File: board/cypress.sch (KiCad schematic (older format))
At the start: 50 parts, among them J1 USB_MICRO_B, U1 CY7C68013A, U2 M25P16, X1 CRYSTAL

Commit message: Issue #1022 - Power supply & pic& SCHEMATIC SECTION.
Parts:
- added R308, R310, R311, R312: 100R, ~, symbol R
- added R309, R313: 330R, ~, symbol R
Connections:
- net at U1.45 (PD0/FD8): now also R308.1
- net at U1.46 (PD1/FD9): now also R309.1
- net at U1.47 (PD2/FD10): now also R310.1
- net at U1.48 (PD3/FD11): now also R311.1
- net at U1.49 (PD4/FD12): now also R312.1
- net RESET: now reaches U1.51 (PD6/FD14)
- net at U1.52 (PD7/FD15): now also R313.1
- new net DONE: R313.2
- new net PROG_B: R309.2
- new net TCK: R312.2
- new net TDO-USB/TDI-FPGA: R310.2
- new net TDO_FPGA/TDO-JTAG: R308.2
- new net TMS: R311.2
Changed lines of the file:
@@
 Sheet 2 8
 Title ""
-Date "14 mar 2014"
+Date "18 mar 2014"
 Rev ""
 Comp ""
@@
 Connection ~ 4600 6900
 NoConn ~ 2050 1650
+$Comp
+L R R308
+U 1 1 5329563E
+P 6100 3450
+F 0 "R308" V 6150 3650 40  0000 C CNN
+F 1 "100R" V 6107 3451 40  0000 C CNN
+F 2 "~" V 6030 3450 30  0000 C CNN
+F 3 "~" H 6100 3450 30  0000 C CNN
+	1    6100 3450
+	0    -1   -1   0
+$EndComp
+Wire Wire Line
+	5600 3450 5850 3450
+Wire Wire Line
+	5600 3650 5850 3650
+$Comp
+L R R310
+U 1 1 53295873
+P 6100 3650
+F 0 "R310" V 6150 3850 40  0000 C CNN
+F 1 "100R" V 6107 3651 40  0000 C CNN
+F 2 "~" V 6030 3650 30  0000 C CNN
+F 3 "~" H 6100 3650 30  0000 C CNN
+	1    6100 3650
+	0    -1   -1   0
+$EndComp
+$Comp
+L R R311
+U 1 1 53295931
+P 6100 3750
+F 0 "R311" V 6150 3950 40  0000 C CNN
+F 1 "100R" V 6107 3751 40  0000 C CNN
+F 2 "~" V 6030 3750 30  0000 C CNN
+F 3 "~" H 6100 3750 30  0000 C CNN
+	1    6100 3750
+	0    -1   -1   0
+$EndComp
+$Comp
+L R R312
+U 1 1 53295964
+P 6100 3850
+F 0 "R312" V 6150 4050 40  0000 C CNN
+F 1 "100R" V 6107 3851 40  0000 C CNN
+F 2 "~" V 6030 3850 30  0000 C CNN
+F 3 "~" H 6100 3850 30  0000 C CNN
+	1    6100 3850
+	0    -1   -1   0
+$EndComp
+Wire Wire Line
+	5600 3750 5850 3750
+Wire Wire Line
+	5600 3850 5850 3850
+Text HLabel 6350 3450 2    39   BiDi ~ 0
+TDO_FPGA/TDO-JTAG
+Text HLabel 6350 3650 2    39   BiDi ~ 0
+TDO-USB/TDI-FPGA
+Text HLabel 6350 3750 2    39   Input ~ 0
+TMS
+Text HLabel 6350 3850 2    39   Input ~ 0
+TCK
+$Comp
+L R R309
+U 1 1 5329986E
+P 6100 3550
+F 0 "R309" V 6150 3750 40  0000 C CNN
+F 1 "330R" V 6107 3551 40  0000 C CNN
+F 2 "~" V 6030 3550 30  0000 C CNN
+F 3 "~" H 6100 3550 30  0000 C CNN
+	1    6100 3550
+	0    -1   -1   0
+$EndComp
+Wire Wire Line
+	5600 3550 5850 3550
+Text HLabel 6350 3550 2    39   Input ~ 0
+PROG_B
+$Comp
+L R R313
+U 1 1 5329AA07
+P 6100 4150
+F 0 "R313" V 6150 4350 40  0000 C CNN
+F 1 "330R" V 6107 4151 40  0000 C CNN
+F 2 "~" V 6030 4150 30  0000 C CNN
+F 3 "~" H 6100 4150 30  0000 C CNN
+	1    6100 4150
+	0    -1   -1   0
+$EndComp
+Wire Wire Line
+	5600 4150 5850 4150
+Text HLabel 6350 4150 2    39   Input ~ 0
+DONE
+Wire Wire Line
+	5600 4050 5900 4050
+Text HLabel 5900 4050 2    39   Input ~ 0
+RESET
 $EndSCHEMATC

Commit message: Issue #1022 - Cypress
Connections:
- no-connect marks 4 -> 5
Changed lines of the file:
@@
 Text HLabel 5900 4050 2    39   Input ~ 0
 RESET
+NoConn ~ 5600 3950
 $EndSCHEMATC

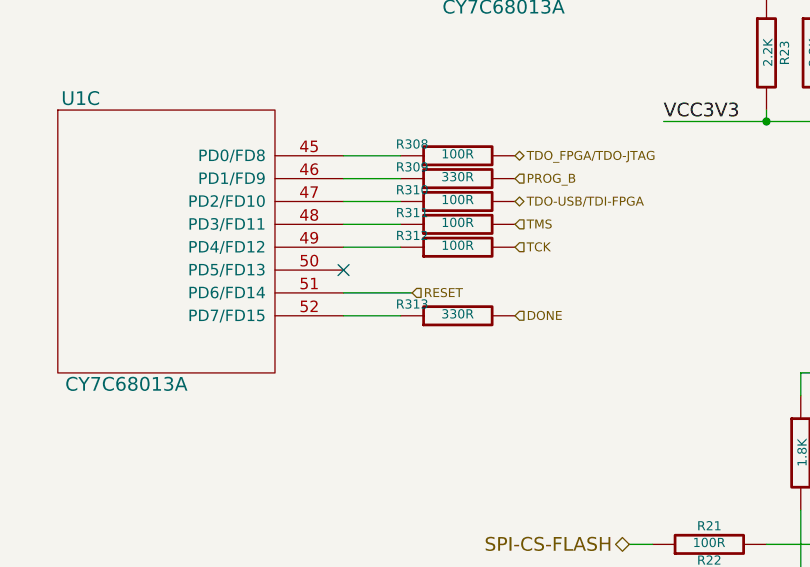
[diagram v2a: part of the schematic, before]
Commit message: Issue #1022 - Reset signals
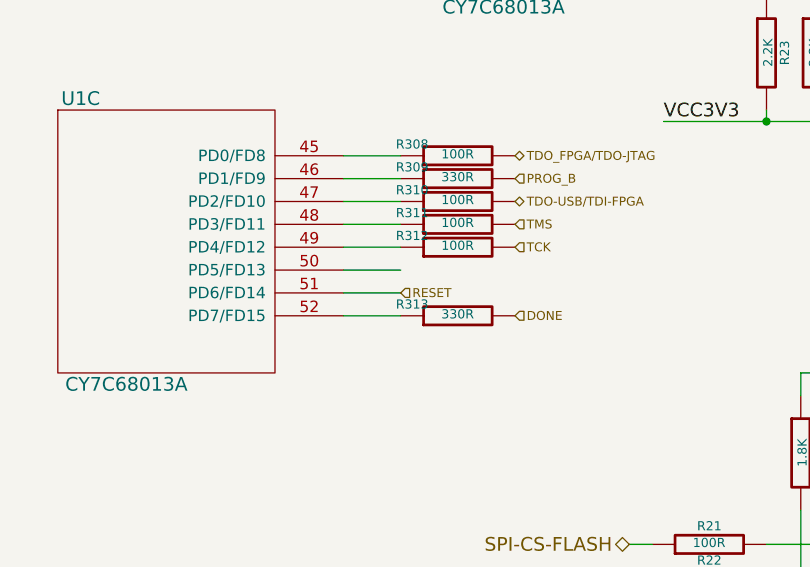
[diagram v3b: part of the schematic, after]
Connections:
- no-connect marks 5 -> 4
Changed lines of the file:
@@
 Sheet 2 8
 Title ""
-Date "18 mar 2014"
+Date "25 mar 2014"
 Rev ""
 Comp ""
@@
 Text HLabel 6350 4150 2    39   Input ~ 0
 DONE
-Wire Wire Line
-	5600 4050 5900 4050
-Text HLabel 5900 4050 2    39   Input ~ 0
+Text HLabel 5850 4050 2    39   Input ~ 0
 RESET
-NoConn ~ 5600 3950
+Wire Wire Line
+	5600 3950 5850 3950
+Wire Wire Line
+	5600 4050 5850 4050
 $EndSCHEMATC

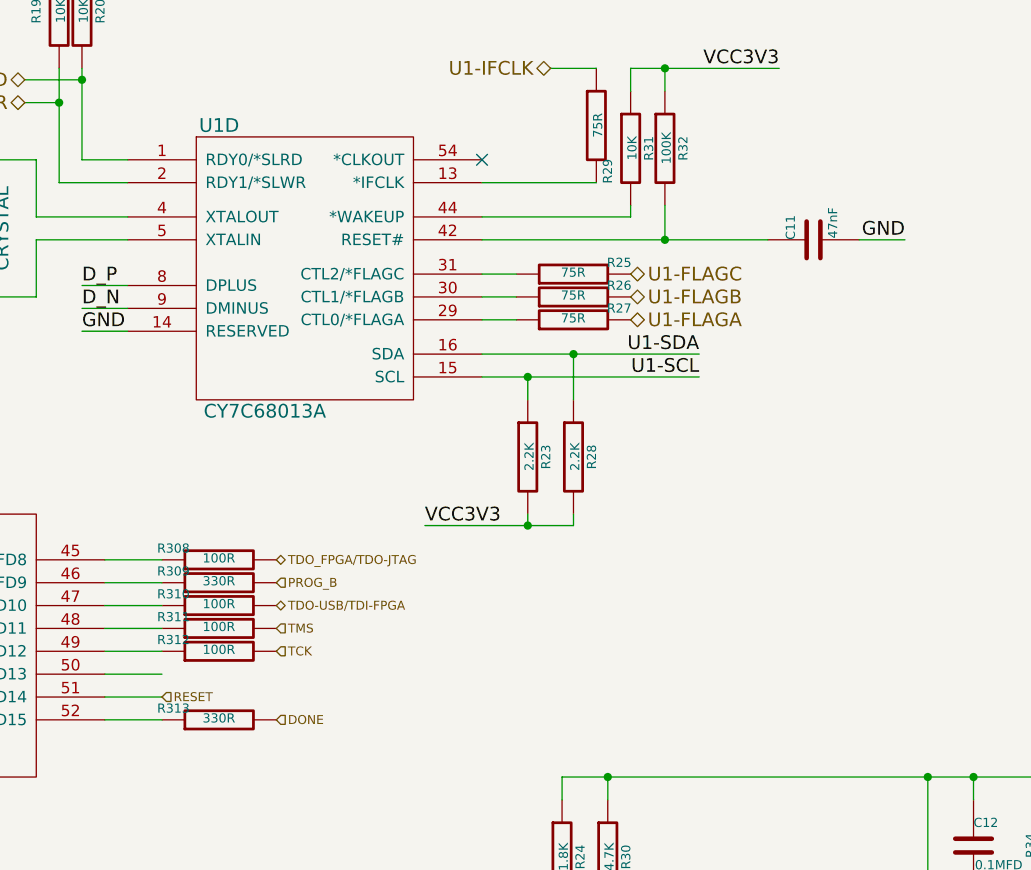
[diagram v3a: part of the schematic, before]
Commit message: Issue #1022 - Reset signals
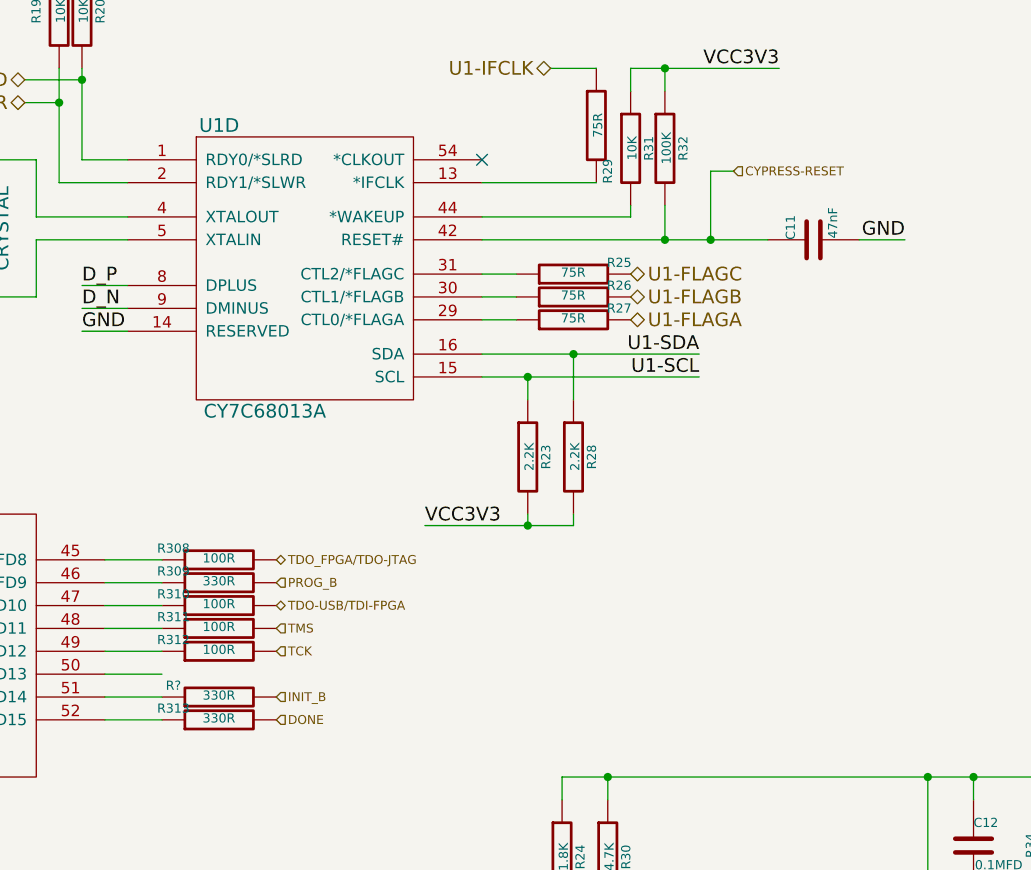
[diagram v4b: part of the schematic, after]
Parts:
- added R?: 330R, ~, symbol R
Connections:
- net CYPRESS-RESET: now reaches C11.1, R32.2, U1.42 (RESET#)
- net RESET: no longer names the net of U1.51 (PD6/FD14)
- net RESET: now also R?.1
- new net INIT_B: R?.2
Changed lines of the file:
@@
 Sheet 2 8
 Title ""
-Date "25 mar 2014"
+Date "26 mar 2014"
 Rev ""
 Comp ""
@@
 Text HLabel 6350 4150 2    39   Input ~ 0
 DONE
-Text HLabel 5850 4050 2    39   Input ~ 0
-RESET
 Wire Wire Line
 	5600 3950 5850 3950
 Wire Wire Line
 	5600 4050 5850 4050
+Wire Wire Line
+	8250 2050 8250 1750
+Wire Wire Line
+	8250 1750 8350 1750
+Connection ~ 8250 2050
+Text HLabel 8350 1750 2    39   Input ~ 0
+CYPRESS-RESET
+Text HLabel 6350 4050 2    39   Input ~ 0
+INIT_B
+$Comp
+L R R?
+U 1 1 53356F60
+P 6100 4050
+F 0 "R?" V 6150 4250 40  0000 C CNN
+F 1 "330R" V 6107 4051 40  0000 C CNN
+F 2 "~" V 6030 4050 30  0000 C CNN
+F 3 "~" H 6100 4050 30  0000 C CNN
+	1    6100 4050
+	0    -1   -1   0
+$EndComp
 $EndSCHEMATC

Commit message: Issue #1022 - RS232,RS422
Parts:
- gave numbers to parts that had none: 1
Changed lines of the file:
@@
 Sheet 2 8
 Title ""
-Date "26 mar 2014"
+Date "28 mar 2014"
 Rev ""
 Comp ""
@@
 $EndComp
 $Comp
-L GND #PWR01
+L GND #PWR1
 U 1 1 51CD0377
 P 3100 6950
-F 0 "#PWR01" H 3100 6950 30  0001 C CNN
+F 0 "#PWR1" H 3100 6950 30  0001 C CNN
 F 1 "GND" H 3100 6880 30  0001 C CNN
 F 2 "" H 3100 6950 60  0000 C CNN
@@
 INIT_B
 $Comp
-L R R?
+L R R289
 U 1 1 53356F60
 P 6100 4050
-F 0 "R?" V 6150 4250 40  0000 C CNN
+F 0 "R289" V 6150 4250 40  0000 C CNN
 F 1 "330R" V 6107 4051 40  0000 C CNN
 F 2 "~" V 6030 4050 30  0000 C CNN

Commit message: Issue #1022 - Schematics final.
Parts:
- added D32: LED, ~, symbol LED
- added R325: 1.8K, ~, symbol R
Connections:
- net GND: now also D32.2 (K)
- net at U1.50 (PD5/FD13): now also R325.1
- new net: D32.1 (A), R325.2
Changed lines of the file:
@@
 Sheet 2 8
 Title ""
-Date "28 mar 2014"
+Date "31 mar 2014"
 Rev ""
 Comp ""
@@
 $EndComp
 $Comp
-L GND #PWR1
+L GND #PWR01
 U 1 1 51CD0377
 P 3100 6950
-F 0 "#PWR1" H 3100 6950 30  0001 C CNN
+F 0 "#PWR01" H 3100 6950 30  0001 C CNN
 F 1 "GND" H 3100 6880 30  0001 C CNN
 F 2 "" H 3100 6950 60  0000 C CNN
@@
 Connection ~ 2850 6350
 Wire Wire Line
-	2850 6450 5300 6450
-Wire Wire Line
-	4850 6500 4850 6450
+	4850 6450 4850 6500
 Connection ~ 4850 6450
 Wire Wire Line
-	4600 6500 4600 6450
+	4600 6450 4600 6500
 Connection ~ 4600 6450
 Wire Wire Line
-	4350 6500 4350 6450
+	4350 6450 4350 6500
 Connection ~ 4350 6450
 Wire Wire Line
-	4100 6500 4100 6450
+	4100 6450 4100 6500
 Connection ~ 4100 6450
 Wire Wire Line
-	3850 6500 3850 6450
+	3850 6450 3850 6500
 Connection ~ 3850 6450
 Wire Wire Line
-	3600 6500 3600 6450
+	3600 6450 3600 6500
 Connection ~ 3600 6450
 Wire Wire Line
@@
 Wire Wire Line
 	3100 6500 3100 6450
-Connection ~ 3100 6450
 Wire Wire Line
 	1300 6900 5450 6900
@@
 DONE
 Wire Wire Line
-	5600 3950 5850 3950
+	5600 3950 6500 3950
 Wire Wire Line
 	5600 4050 5850 4050
@@
 	0    -1   -1   0
 $EndComp
+$Comp
+L LED D32
+U 1 1 533E43EE
+P 7250 3950
+F 0 "D32" H 7250 4050 50  0000 C CNN
+F 1 "LED" H 7250 3850 50  0000 C CNN
+F 2 "~" H 7250 3950 60  0000 C CNN
+F 3 "~" H 7250 3950 60  0000 C CNN
+	1    7250 3950
+	1    0    0    -1
+$EndComp
+$Comp
+L R R325
+U 1 1 533E70A1
+P 6750 3950
+F 0 "R325" V 6830 3950 40  0000 C CNN
+F 1 "1.8K" V 6757 3951 40  0000 C CNN
+F 2 "~" V 6680 3950 30  0000 C CNN
+F 3 "~" H 6750 3950 30  0000 C CNN
+	1    6750 3950
+	0    -1   -1   0
+$EndComp
+Wire Wire Line
+	7050 3950 7000 3950
+Text Label 7650 3950 2    60   ~ 0
+GND
+Wire Wire Line
+	7450 3950 7650 3950
+Text Label 3200 5700 2    60   ~ 0
+VCC3V3
+Wire Wire Line
+	2850 5700 3200 5700
+Wire Wire Line
+	3100 6450 5300 6450
 $EndSCHEMATC

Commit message: Issue #993
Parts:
- removed C12: 0.1MFD, ~, symbol C
- removed R21, R22, R33: 100R, ~, symbol R
- removed R24, R34: 1.8K, ~, symbol R
- removed R30: 4.7K, ~, symbol R
- removed U2: M25P16, symbol M25P16
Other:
- moved on the sheet: C1, C10, C11, C2, C3, C4, C5, C6, C7, C8, C9, D32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

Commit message: Issue #1022 - Schematics final changes.
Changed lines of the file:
@@
 Sheet 6 8
 Title "HDMI2USB"
-Date "3 apr 2014"
+Date "7 apr 2014"
 Rev ""
 Comp ""
@@
 Connection ~ 8500 3450
 Wire Wire Line
-	9350 3450 9550 3450
-Wire Wire Line
 	5750 3350 6150 3350
 Wire Wire Line
@@
 	7750 6150 8000 6150
 Wire Wire Line
-	8700 3450 8700 3150
-Wire Wire Line
-	8700 3150 8800 3150
+	8700 3000 8700 3450
 Connection ~ 8700 3450
-Text HLabel 8800 3150 2    39   Input ~ 0
+Text HLabel 8750 3000 2    39   Input ~ 0
 CYPRESS-RESET
 Text HLabel 8500 6150 2    39   Input ~ 0
@@
 Wire Wire Line
 	3050 6650 5250 6650
+Wire Wire Line
+	8700 3000 8750 3000
+Wire Wire Line
+	9350 3450 9550 3450
 $EndSCHEMATC
